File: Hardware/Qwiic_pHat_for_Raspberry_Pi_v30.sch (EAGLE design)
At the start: 24 parts, among them J1 Qwiic Right Angle, J10 RASPBERRYPI-40-PIN-GPIO_PTH_N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, J7 Qwiic Right Angle, J8 Qwiic Right Angle

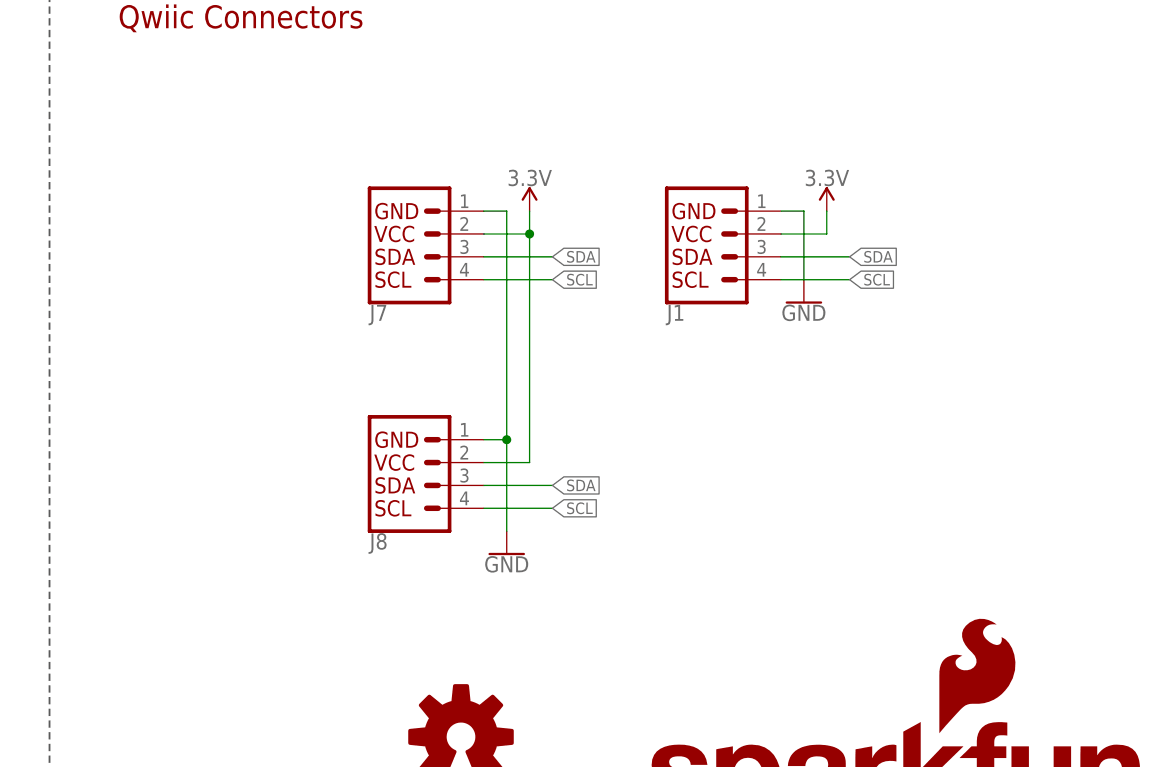
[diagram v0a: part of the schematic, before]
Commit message: Adds vertical Qwiic connectors to board
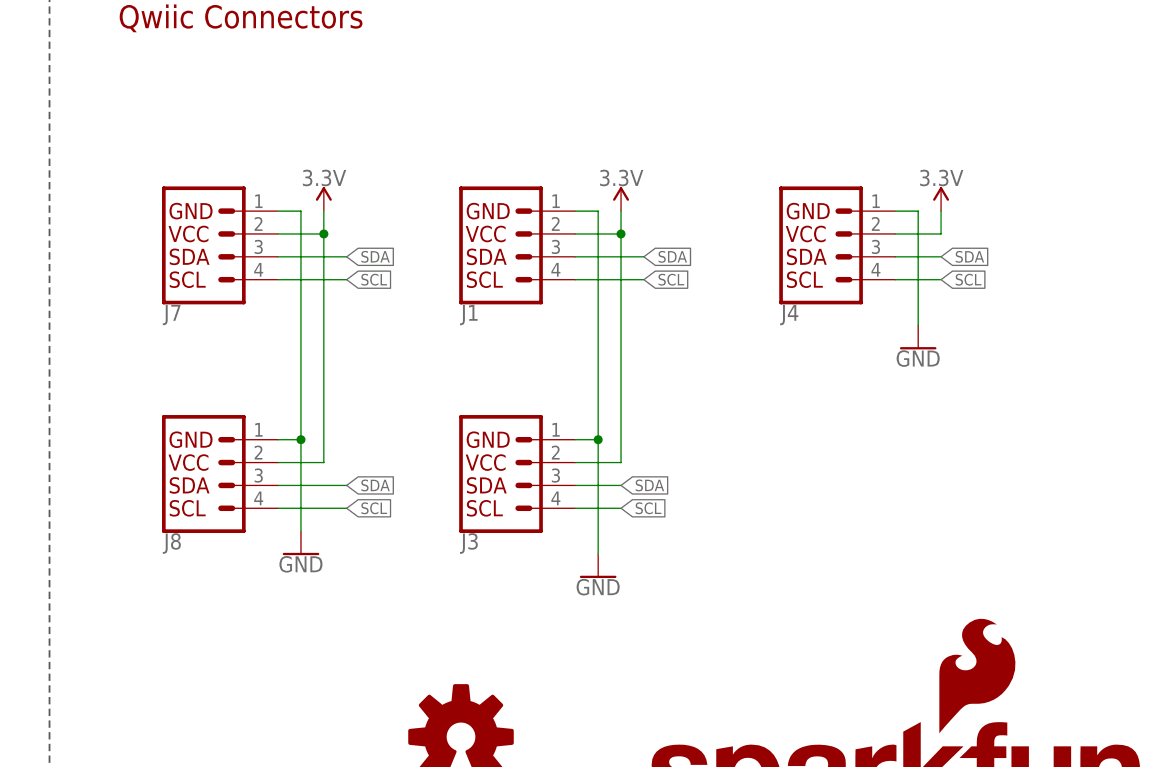
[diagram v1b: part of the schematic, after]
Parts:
- added J3, J4: (no value), SparkFun-Connectors:QWIIC_CONNECTOR
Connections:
- net 3.3V: now also J3.2, J4.2
- net GND: now also J3.1, J4.1
- net SCL: now also J3.4, J4.4
- net SDA: now also J3.3, J4.3
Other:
- moved on the sheet: J1, J7, J8

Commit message: Updates vertical qwiic connector footprint, recenters vertical qwiic connector.
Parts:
- LOGO1: value SFE_LOGO_NAME_FLAME.2_INCH -> SFE_LOGO_NAME_FLAME.1_INCH; device SparkFun-Aesthetics:SFE_LOGO_NAME_FLAME.2_INCH -> SparkFun-Aesthetics:SFE_LOGO_NAME_FLAME.1_INCH
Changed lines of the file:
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@@
 <layer number="115" name="ReferenceISLANDS" color="7" fill="1" visible="yes" active="yes"/>
 <layer number="116" name="Patch_BOT" color="9" fill="4" visible="yes" active="yes"/>
+<layer number="117" name="PM_Ref" color="26" fill="1" visible="yes" active="yes"/>
 <layer number="118" name="Rect_Pads" color="7" fill="1" visible="yes" active="yes"/>
+<layer number="119" name="PF_Ref" color="31" fill="1" visible="yes" active="yes"/>
+<layer number="120" name="WFL_Ref" color="25" fill="1" visible="yes" active="yes"/>
 <layer number="121" name="_tsilk" color="7" fill="1" visible="yes" active="yes"/>
 <layer number="122" name="_bsilk" color="7" fill="1" visible="yes" active="yes"/>
@@
 <part name="H5" library="SparkFun-Hardware" deviceset="STAND-OFF" device="TIGHT"/>
 <part name="H6" library="SparkFun-Hardware" deviceset="STAND-OFF" device="TIGHT"/>
-<part name="LOGO1" library="SparkFun-Aesthetics" deviceset="SFE_LOGO_NAME_FLAME" device=".2_INCH"/>
+<part name="LOGO1" library="SparkFun-Aesthetics" deviceset="SFE_LOGO_NAME_FLAME" device=".1_INCH" value="SFE_LOGO_NAME_FLAME.1_INCH"/>
 <part name="LOGO3" library="SparkFun-Aesthetics" deviceset="OSHW-LOGO" device="S" value="OSHW-LOGOS"/>
 <part name="JP1" library="SparkFun-Jumpers" deviceset="JUMPER-SMT_3_2-NC_TRACE" device="_NO-SILK" value="PULLUP"/>

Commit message: Changes button and 5V power labels to text only, changes button text to "button" with gpio number
* Adds parallel 5V power through holes
* moves + and - silk
* moves button gpio pin to 17
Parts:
- removed J7: Qwiic Right Angle, SparkFun-Connectors:I2C_STANDARDQWIIC
- added J5: (no value), SparkFun-Connectors:CONN_023.5MM-NO_SILK
- J2: device SparkFun-Connectors:CONN_023.5MM-NO_SILK -> SparkFun-Connectors:CONN_023.5MM
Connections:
- net 3.3V: no longer J7.2
- net 5V: now also J5.1
- net D17: now also R3.1, S1.2
- net D19: no longer R3.1, S1.2
- net GND: now also J5.2; no longer J7.1
- net SCL: no longer J7.4
- net SDA: no longer J7.3
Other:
- moved on the sheet: J8
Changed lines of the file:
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@@
 <part name="SUPPLY5" library="SparkFun-PowerSymbols" deviceset="3.3V" device=""/>
 <part name="GND6" library="SparkFun-PowerSymbols" deviceset="GND" device=""/>
-<part name="J7" library="SparkFun-Connectors" deviceset="I2C_STANDARD" device="QWIIC" value="Qwiic Right Angle"/>
-<part name="SUPPLY7" library="SparkFun-PowerSymbols" deviceset="3.3V" device=""/>
 <part name="J8" library="SparkFun-Connectors" deviceset="I2C_STANDARD" device="QWIIC" value="Qwiic Right Angle"/>
 <part name="GND8" library="SparkFun-PowerSymbols" deviceset="GND" device=""/>
@@
 <part name="R2" library="SparkFun-Resistors" deviceset="2.2KOHM" device="-0603-1/10W-1%" value="2.2k"/>
 <part name="SUPPLY2" library="SparkFun-PowerSymbols" deviceset="3.3V" device=""/>
-<part name="J2" library="SparkFun-Connectors" deviceset="CONN_02" device="3.5MM-NO_SILK"/>
+<part name="J2" library="SparkFun-Connectors" deviceset="CONN_02" device="3.5MM"/>
 <part name="GND1" library="SparkFun-PowerSymbols" deviceset="GND" device=""/>
 <part name="SUPPLY3" library="SparkFun-PowerSymbols" deviceset="5V" device=""/>
@@
 <part name="GND3" library="SparkFun-PowerSymbols" deviceset="GND" device=""/>
 <part name="SUPPLY6" library="SparkFun-PowerSymbols" deviceset="3.3V" device=""/>
+<part name="J5" library="SparkFun-Connectors" deviceset="CONN_02" device="3.5MM-NO_SILK"/>
 </parts>
 <sheets>
@@
 <plain>
 <text x="168.148" y="11.43" size="2.54" layer="94" font="vector">N. Seidle</text>
-<text x="10.16" y="119.38" size="2.54" layer="94" font="vector" ratio="12">Raspberry Pi Connector</text>
+<text x="5.08" y="124.46" size="2.54" layer="94" font="vector" ratio="12">Raspberry Pi Connector</text>
 <text x="238.76" y="7.62" size="1.778" layer="94" font="vector" ratio="12">V30</text>
 <text x="129.54" y="124.46" size="2.54" layer="94" font="vector" ratio="12">Qwiic Connectors</text>
@@
 <attribute name="VALUE" x="182.88" y="63.246" size="1.778" layer="96" align="top-center"/>
 </instance>
-<instance part="J7" gate="G$1" x="139.7" y="101.6" smashed="yes" rot="MR180">
-<attribute name="NAME" x="134.62" y="93.726" size="1.778" layer="95" font="vector" rot="MR180"/>
-</instance>
-<instance part="SUPPLY7" gate="G$1" x="152.4" y="104.14" smashed="yes">
-<attribute name="VALUE" x="152.4" y="106.934" size="1.778" layer="96" align="bottom-center"/>
-</instance>
-<instance part="J8" gate="G$1" x="139.7" y="76.2" smashed="yes" rot="MR180">
-<attribute name="NAME" x="134.62" y="68.326" size="1.778" layer="95" font="vector" rot="MR180"/>
-</instance>
-<instance part="GND8" gate="1" x="149.86" y="66.04" smashed="yes">
-<attribute name="VALUE" x="149.86" y="65.786" size="1.778" layer="96" align="top-center"/>
+<instance part="J8" gate="G$1" x="208.28" y="73.66" smashed="yes" rot="MR180">
+<attribute name="NAME" x="203.2" y="65.786" size="1.778" layer="95" font="vector" rot="MR180"/>
+</instance>
+<instance part="GND8" gate="1" x="218.44" y="63.5" smashed="yes">
+<attribute name="VALUE" x="218.44" y="63.246" size="1.778" layer="96" align="top-center"/>
 </instance>
 <instance part="FD3" gate="G$1" x="246.38" y="27.94" smashed="yes"/>
@@
 <attribute name="VALUE" x="220.98" y="106.934" size="1.778" layer="96" align="bottom-center"/>
 </instance>
+<instance part="J5" gate="G$1" x="139.7" y="157.48" smashed="yes" rot="MR180">
+<attribute name="VALUE" x="137.16" y="162.306" size="1.778" layer="96" font="vector" rot="MR180"/>
+<attribute name="NAME" x="137.16" y="151.892" size="1.778" layer="95" font="vector" rot="MR180"/>
+</instance>
 </instances>
 <busses>
@@
 <segment>
 <pinref part="J8" gate="G$1" pin="1"/>
-<wire x1="147.32" y1="78.74" x2="149.86" y2="78.74" width="0.1524" layer="91"/>
-<wire x1="149.86" y1="78.74" x2="149.86" y2="68.58" width="0.1524" layer="91"/>
+<wire x1="215.9" y1="76.2" x2="218.44" y2="76.2" width="0.1524" layer="91"/>
+<wire x1="218.44" y1="76.2" x2="218.44" y2="66.04" width="0.1524" layer="91"/>
 <pinref part="GND8" gate="1" pin="GND"/>
-<pinref part="J7" gate="G$1" pin="1"/>
-<wire x1="147.32" y1="104.14" x2="149.86" y2="104.14" width="0.1524" layer="91"/>
-<wire x1="149.86" y1="104.14" x2="149.86" y2="78.74" width="0.1524" layer="91"/>
-<junction x="149.86" y="78.74"/>
 </segment>
 <segment>
@@
 <wire x1="149.86" y1="154.94" x2="149.86" y2="152.4" width="0.1524" layer="91"/>
 <pinref part="GND1" gate="1" pin="GND"/>
+<pinref part="J5" gate="G$1" pin="2"/>
+<wire x1="147.32" y1="154.94" x2="149.86" y2="154.94" width="0.1524" layer="91"/>
+<junction x="149.86" y="154.94"/>
 </segment>
 <segment>
@@
 </segment>
 <segment>
-<pinref part="J7" gate="G$1" pin="2"/>
-<wire x1="147.32" y1="101.6" x2="152.4" y2="101.6" width="0.1524" layer="91"/>
-<wire x1="152.4" y1="101.6" x2="152.4" y2="104.14" width="0.1524" layer="91"/>
-<pinref part="SUPPLY7" gate="G$1" pin="3.3V"/>
-<pinref part="J8" gate="G$1" pin="2"/>
-<wire x1="147.32" y1="76.2" x2="152.4" y2="76.2" width="0.1524" layer="91"/>
-<wire x1="152.4" y1="76.2" x2="152.4" y2="101.6" width="0.1524" layer="91"/>
-<junction x="152.4" y="101.6"/>
-</segment>
-<segment>
 <pinref part="JP1" gate="G$1" pin="2"/>
 <wire x1="66.04" y1="154.94" x2="71.12" y2="154.94" width="0.1524" layer="91"/>
@@
 <wire x1="220.98" y1="101.6" x2="220.98" y2="104.14" width="0.1524" layer="91"/>
 <pinref part="SUPPLY6" gate="G$1" pin="3.3V"/>
+<pinref part="J8" gate="G$1" pin="2"/>
+<wire x1="215.9" y1="73.66" x2="220.98" y2="73.66" width="0.1524" layer="91"/>
+<wire x1="220.98" y1="73.66" x2="220.98" y2="101.6" width="0.1524" layer="91"/>
+<junction x="220.98" y="101.6"/>
 </segment>
 </net>
@@
 </segment>
 <segment>
-<pinref part="J7" gate="G$1" pin="3"/>
-<wire x1="147.32" y1="99.06" x2="154.94" y2="99.06" width="0.1524" layer="91"/>
-<label x="154.94" y="99.06" size="1.27" layer="95" xref="yes"/>
-</segment>
-<segment>
 <pinref part="J8" gate="G$1" pin="3"/>
-<wire x1="147.32" y1="73.66" x2="154.94" y2="73.66" width="0.1524" layer="91"/>
-<label x="154.94" y="73.66" size="1.27" layer="95" xref="yes"/>
+<wire x1="215.9" y1="71.12" x2="220.98" y2="71.12" width="0.1524" layer="91"/>
+<label x="220.98" y="71.12" size="1.27" layer="95" xref="yes"/>
 </segment>
 <segment>
@@
 <segment>
 <pinref part="J4" gate="G$1" pin="3"/>
-<wire x1="215.9" y1="99.06" x2="220.98" y2="99.06" width="0.1524" layer="91"/>
-<label x="220.98" y="99.06" size="1.27" layer="95" xref="yes"/>
+<wire x1="215.9" y1="99.06" x2="223.52" y2="99.06" width="0.1524" layer="91"/>
+<label x="223.52" y="99.06" size="1.27" layer="95" xref="yes"/>
 </segment>
 </net>
@@
 </segment>
 <segment>
-<pinref part="J7" gate="G$1" pin="4"/>
-<wire x1="147.32" y1="96.52" x2="154.94" y2="96.52" width="0.1524" layer="91"/>
-<label x="154.94" y="96.52" size="1.27" layer="95" xref="yes"/>
-</segment>
-<segment>
 <pinref part="J8" gate="G$1" pin="4"/>
-<wire x1="147.32" y1="71.12" x2="154.94" y2="71.12" width="0.1524" layer="91"/>
-<label x="154.94" y="71.12" size="1.27" layer="95" xref="yes"/>
+<wire x1="215.9" y1="68.58" x2="220.98" y2="68.58" width="0.1524" layer="91"/>
+<label x="220.98" y="68.58" size="1.27" layer="95" xref="yes"/>
 </segment>
 <segment>
@@
 <segment>
 <pinref part="J4" gate="G$1" pin="4"/>
-<wire x1="215.9" y1="96.52" x2="220.98" y2="96.52" width="0.1524" layer="91"/>
-<label x="220.98" y="96.52" size="1.27" layer="95" xref="yes"/>
+<wire x1="215.9" y1="96.52" x2="223.52" y2="96.52" width="0.1524" layer="91"/>
+<label x="223.52" y="96.52" size="1.27" layer="95" xref="yes"/>
 </segment>
 </net>
@@
 <wire x1="149.86" y1="157.48" x2="149.86" y2="160.02" width="0.1524" layer="91"/>
 <pinref part="SUPPLY3" gate="G$1" pin="5V"/>
+<pinref part="J5" gate="G$1" pin="1"/>
+<wire x1="147.32" y1="157.48" x2="149.86" y2="157.48" width="0.1524" layer="91"/>
+<junction x="149.86" y="157.48"/>
 </segment>
 </net>
@@
 <wire x1="68.58" y1="58.42" x2="71.12" y2="58.42" width="0.1524" layer="91"/>
 <label x="71.12" y="58.42" size="1.27" layer="95" font="vector" xref="yes"/>
-</segment>
-</net>
-<net name="D18" class="0">
-<segment>
-<pinref part="J10" gate="G$1" pin="GP18#"/>
-<wire x1="68.58" y1="55.88" x2="71.12" y2="55.88" width="0.1524" layer="91"/>
-<label x="71.12" y="55.88" size="1.27" layer="95" font="vector" xref="yes"/>
-</segment>
-</net>
-<net name="D19" class="0">
-<segment>
-<pinref part="J10" gate="G$1" pin="GP19"/>
-<wire x1="38.1" y1="66.04" x2="35.56" y2="66.04" width="0.1524" layer="91"/>
-<label x="35.56" y="66.04" size="1.27" layer="95" font="vector" rot="R180" xref="yes"/>
 </segment>
 <segment>
@@
 </segment>
 </net>
+<net name="D18" class="0">
+<segment>
+<pinref part="J10" gate="G$1" pin="GP18#"/>
+<wire x1="68.58" y1="55.88" x2="71.12" y2="55.88" width="0.1524" layer="91"/>
+<label x="71.12" y="55.88" size="1.27" layer="95" font="vector" xref="yes"/>
+</segment>
+</net>
+<net name="D19" class="0">
+<segment>
+<pinref part="J10" gate="G$1" pin="GP19"/>
+<wire x1="38.1" y1="66.04" x2="35.56" y2="66.04" width="0.1524" layer="91"/>
+<label x="35.56" y="66.04" size="1.27" layer="95" font="vector" rot="R180" xref="yes"/>
+</segment>
+</net>

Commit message: Adjusts 5V Power silk, changes button name in schematic
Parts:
- S1: value POWER_OFF -> BUTTON GPI017
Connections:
- net D17 renamed BUTTON/D17
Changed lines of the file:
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@@
 <part name="GND1" library="SparkFun-PowerSymbols" deviceset="GND" device=""/>
 <part name="SUPPLY3" library="SparkFun-PowerSymbols" deviceset="5V" device=""/>
-<part name="S1" library="SparkFun-Switches" deviceset="MOMENTARY-SWITCH-SPST" device="-SMD-5.2MM-TALL" value="POWER_OFF"/>
+<part name="S1" library="SparkFun-Switches" deviceset="MOMENTARY-SWITCH-SPST" device="-SMD-5.2MM-TALL" value="BUTTON GPI017"/>
 <part name="GND2" library="SparkFun-PowerSymbols" deviceset="GND" device=""/>
 <part name="R3" library="SparkFun-Resistors" deviceset="10KOHM" device="-0603-1/10W-1%" value="10k"/>
@@
 </segment>
 </net>
-<net name="D17" class="0">
+<net name="BUTTON/D17" class="0">
 <segment>
 <pinref part="J10" gate="G$1" pin="GP17"/>
